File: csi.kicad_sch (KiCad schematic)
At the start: 26 parts, among them J15 Bus_DDR4_SODIMM_CUSTOM_Jetson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, T8 BSS138PW, U10 TPS7A0528PDBVR, U11 TLV75512PDBVR, U4 PCA9547_VQFN

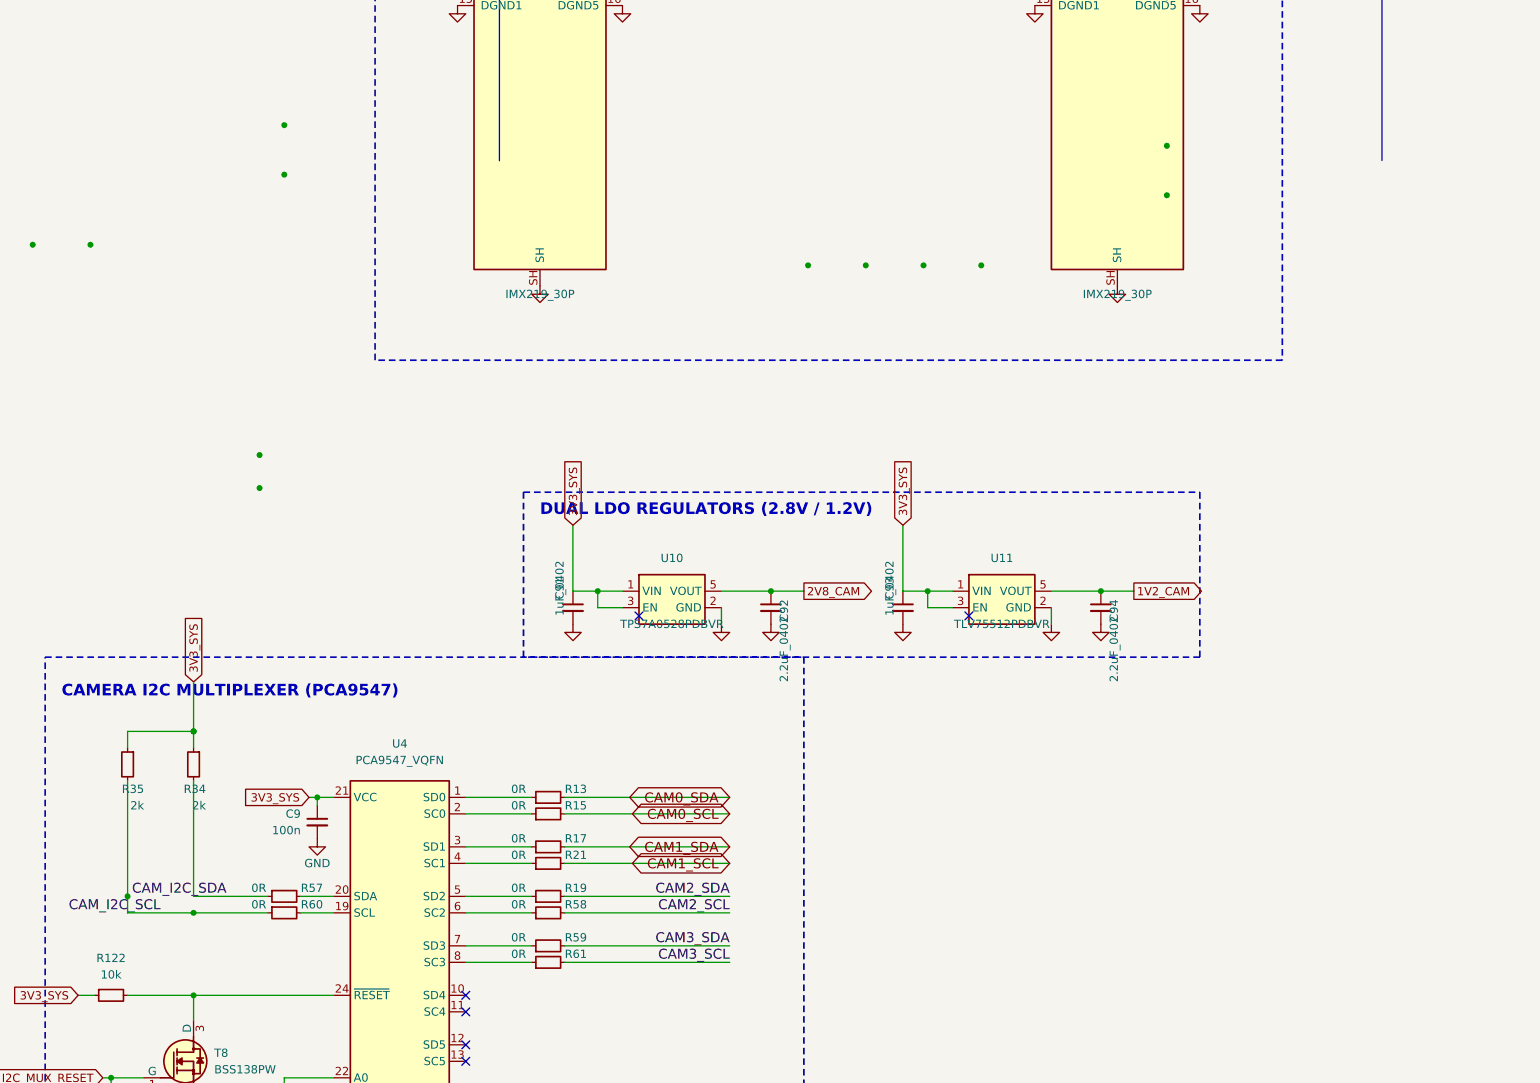
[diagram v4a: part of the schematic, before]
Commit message: fix(csi): upgrade U11 to TLV75512, add local decoupling, I2C pull-ups, PWDN pull-downs, and DNP R34/R35
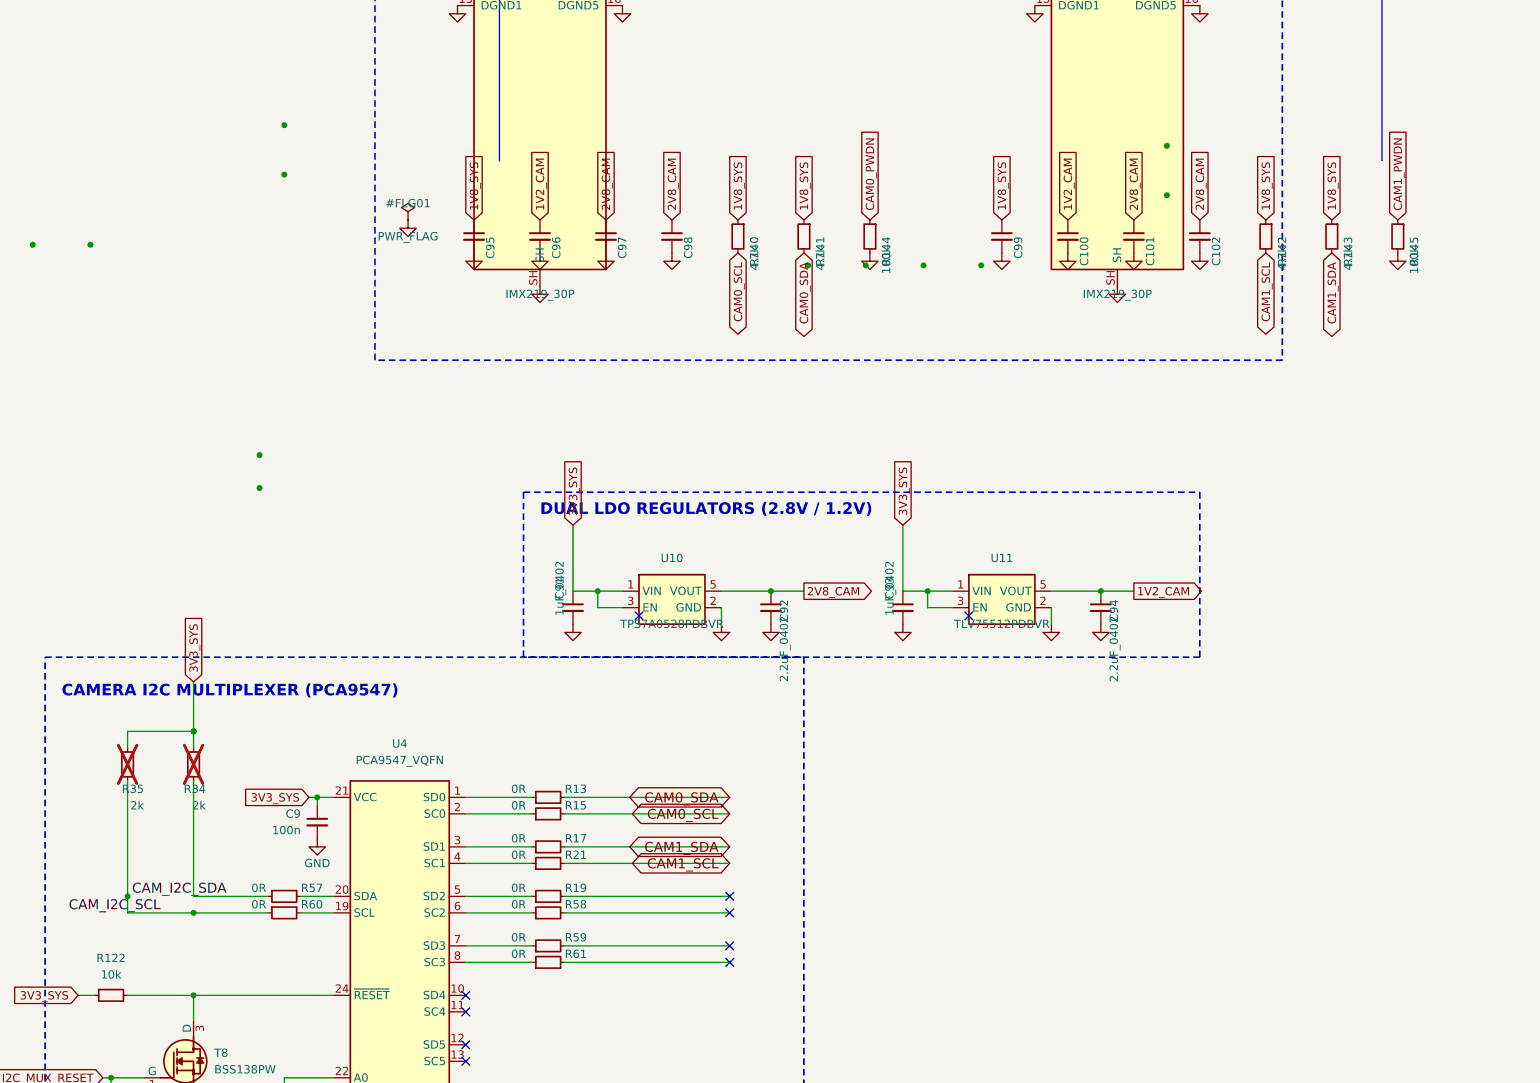
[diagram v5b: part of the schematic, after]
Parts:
- added C100, C101, C95, C96, C97, C99: C_100n_0402, jetson-footprints:C_0402_1005Metric, symbol jetson-symbols:C_100n_0402
- added C102, C98: C_2u2_0402, jetson-footprints:C_0402_1005Metric, symbol jetson-symbols:C_2u2_0402
- added R140, R141, R142, R143: 4.7k, jetson-footprints:R_0402_1005Metric, symbol jetson-symbols:R_2k_0402
- added R144, R145: 100k, jetson-footprints:R_0402_1005Metric, symbol jetson-symbols:R_100k_0402
- R34, R35: now not fitted; now left out of the parts list
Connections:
- net 1V2_CAM: now also C100.1, C96.1
- net 1V8_SYS: now also C95.1, C99.1, R140.1, R141.1, R142.1, R143.1
- net 2V8_CAM: now also C101.1, C102.1, C97.1, C98.1
- net CAM0_PWDN: now also R144.1
- net CAM0_SCL: now also R140.2
- net CAM0_SDA: now also R141.2
- net CAM1_PWDN: now also R145.1
- net CAM1_SCL: now also R142.2
- net CAM1_SDA: now also R143.2
- net GND: now also C100.2, C101.2, C102.2, C95.2, C96.2, C97.2, C98.2, C99.2, R144.2, R145.2
- net CAM2_SCL: no longer names the net of R58.2
- net CAM2_SDA: no longer names the net of R19.2
- net CAM3_SCL: no longer names the net of R61.2
- net CAM3_SDA: no longer names the net of R59.2
- no-connect marks 28 -> 32

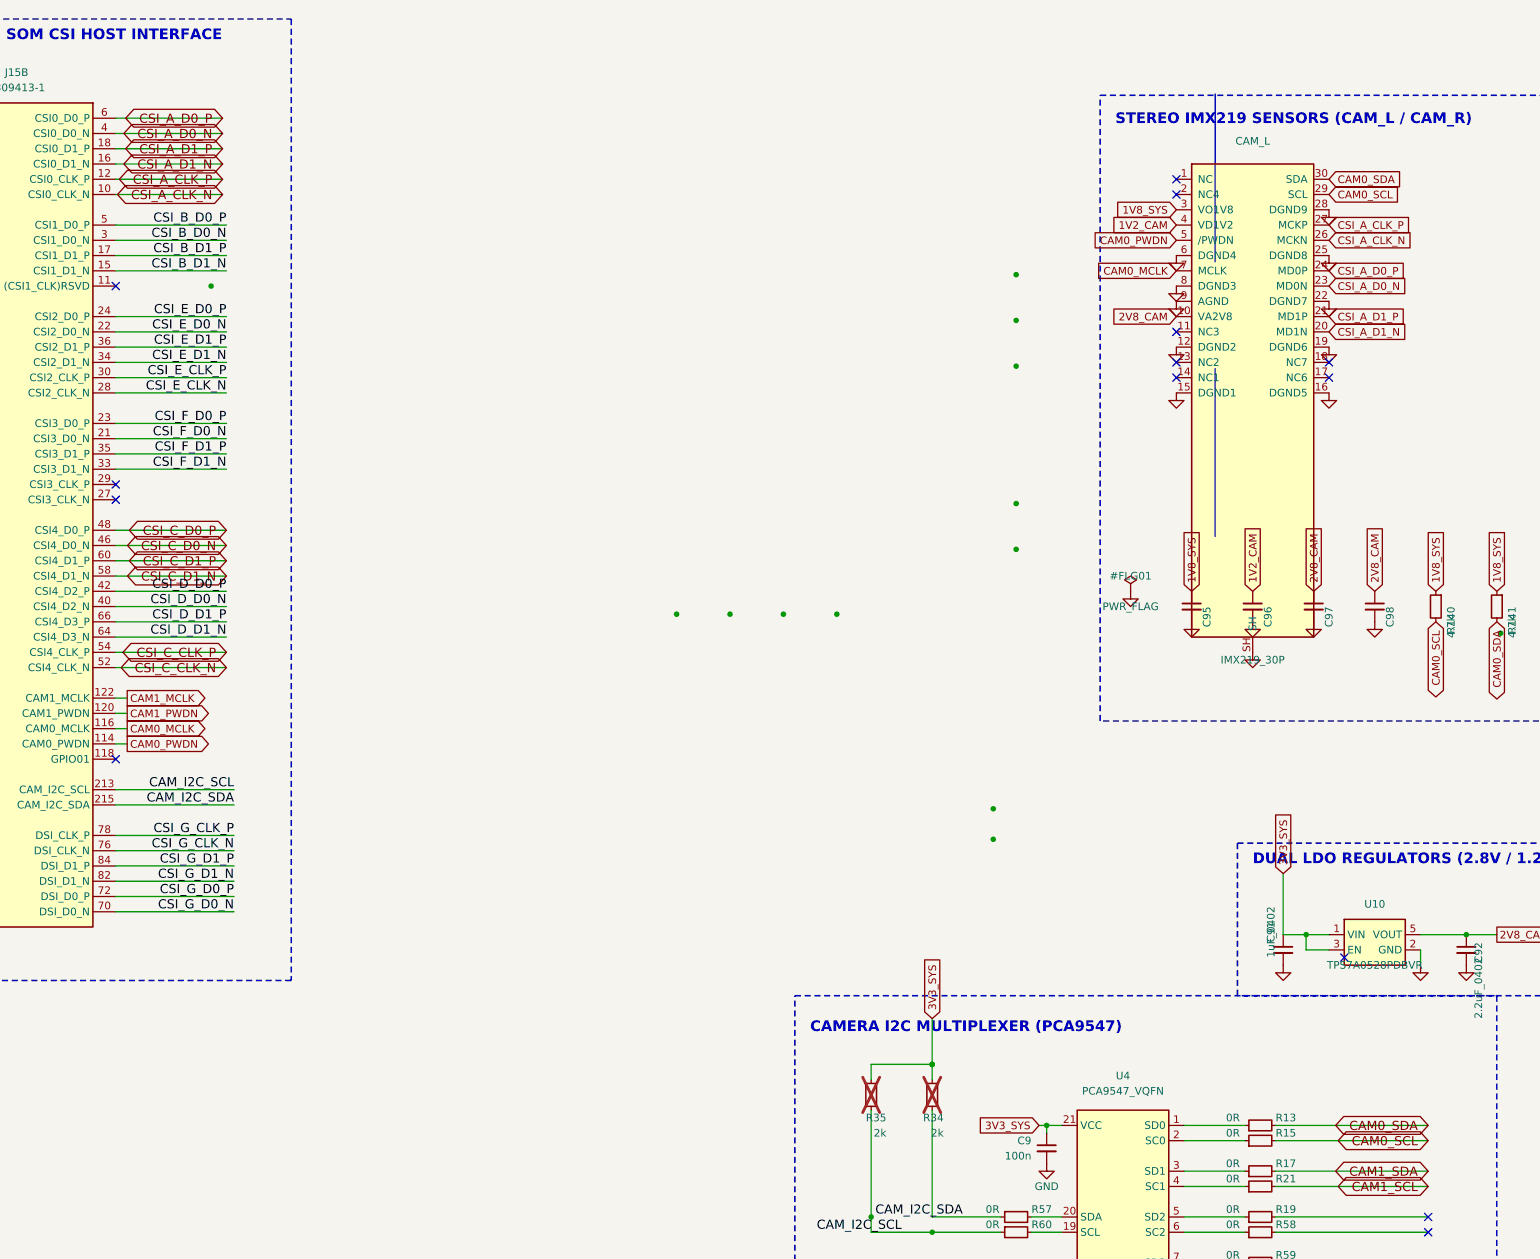
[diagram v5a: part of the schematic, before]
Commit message: fix(phase1): resolve all schematic defects across som, usb, supply, csi, id-serial with zero ERC errors
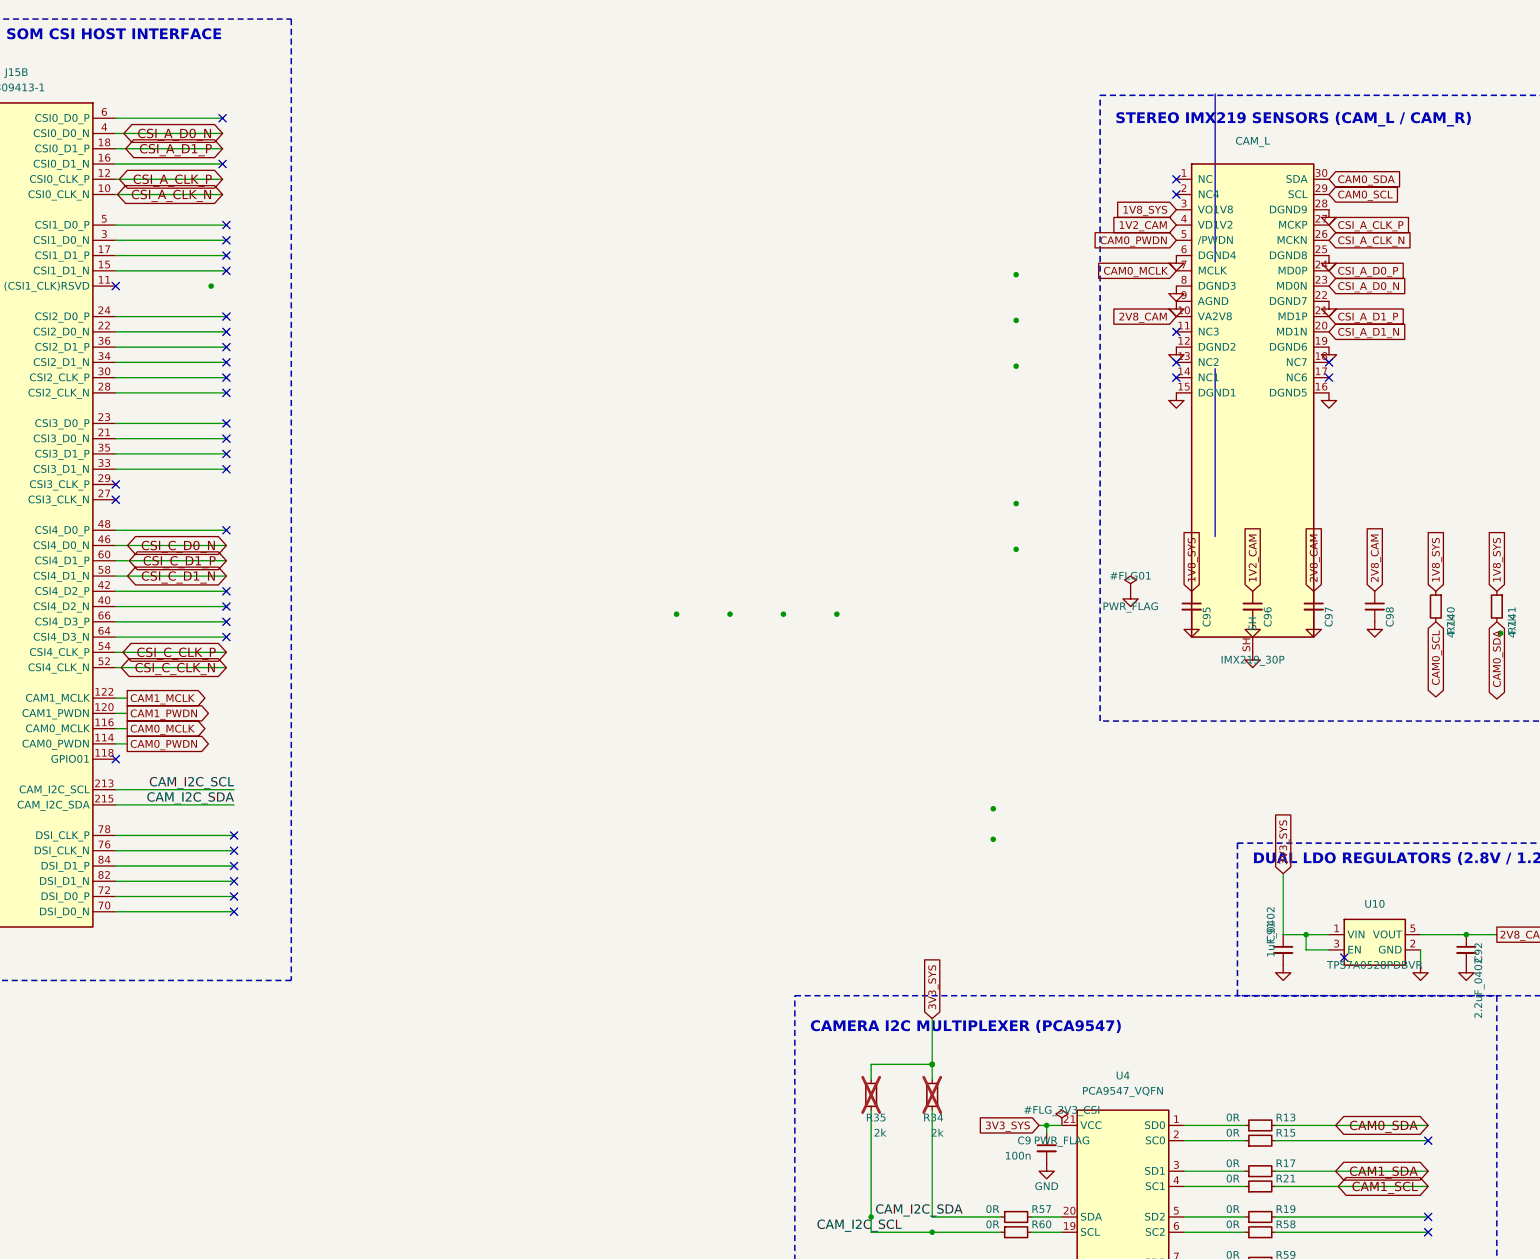
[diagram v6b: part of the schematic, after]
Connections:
- net CAM0_SCL: no longer R15.2
- net CSI_A_D0_P: no longer J15.6 (CSI0_D0_P)
- net CSI_A_D1_N: no longer J15.16 (CSI0_D1_N)
- net CSI_C_D0_P: no longer J15.48 (CSI4_D0_P)
- net CSI_B_D0_N: no longer names the net of J15.3 (CSI1_D0_N)
- net CSI_B_D0_P: no longer names the net of J15.5 (CSI1_D0_P)
- net CSI_B_D1_N: no longer names the net of J15.15 (CSI1_D1_N)
- net CSI_B_D1_P: no longer names the net of J15.17 (CSI1_D1_P)
- net CSI_D_D0_N: no longer names the net of J15.40 (CSI4_D2_N)
- net CSI_D_D0_P: no longer names the net of J15.42 (CSI4_D2_P)
- net CSI_D_D1_N: no longer names the net of J15.64 (CSI4_D3_N)
- net CSI_D_D1_P: no longer names the net of J15.66 (CSI4_D3_P)
- net CSI_E_CLK_N: no longer names the net of J15.28 (CSI2_CLK_N)
- net CSI_E_CLK_P: no longer names the net of J15.30 (CSI2_CLK_P)
- net CSI_E_D0_N: no longer names the net of J15.22 (CSI2_D0_N)
- net CSI_E_D0_P: no longer names the net of J15.24 (CSI2_D0_P)
- net CSI_E_D1_N: no longer names the net of J15.34 (CSI2_D1_N)
- net CSI_E_D1_P: no longer names the net of J15.36 (CSI2_D1_P)
- net CSI_F_D0_N: no longer names the net of J15.21 (CSI3_D0_N)
- net CSI_F_D0_P: no longer names the net of J15.23 (CSI3_D0_P)
- net CSI_F_D1_N: no longer names the net of J15.33 (CSI3_D1_N)
- net CSI_F_D1_P: no longer names the net of J15.35 (CSI3_D1_P)
- net CSI_G_CLK_N: no longer names the net of J15.76 (DSI_CLK_N)
- net CSI_G_CLK_P: no longer names the net of J15.78 (DSI_CLK_P)
- net CSI_G_D0_N: no longer names the net of J15.70 (DSI_D0_N)
- net CSI_G_D0_P: no longer names the net of J15.72 (DSI_D0_P)
- net CSI_G_D1_N: no longer names the net of J15.82 (DSI_D1_N)
- net CSI_G_D1_P: no longer names the net of J15.84 (DSI_D1_P)
- no-connect marks 32 -> 60
